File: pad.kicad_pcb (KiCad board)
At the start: 2 copper layers, 142.7 x 72.9 mm, 0 parts

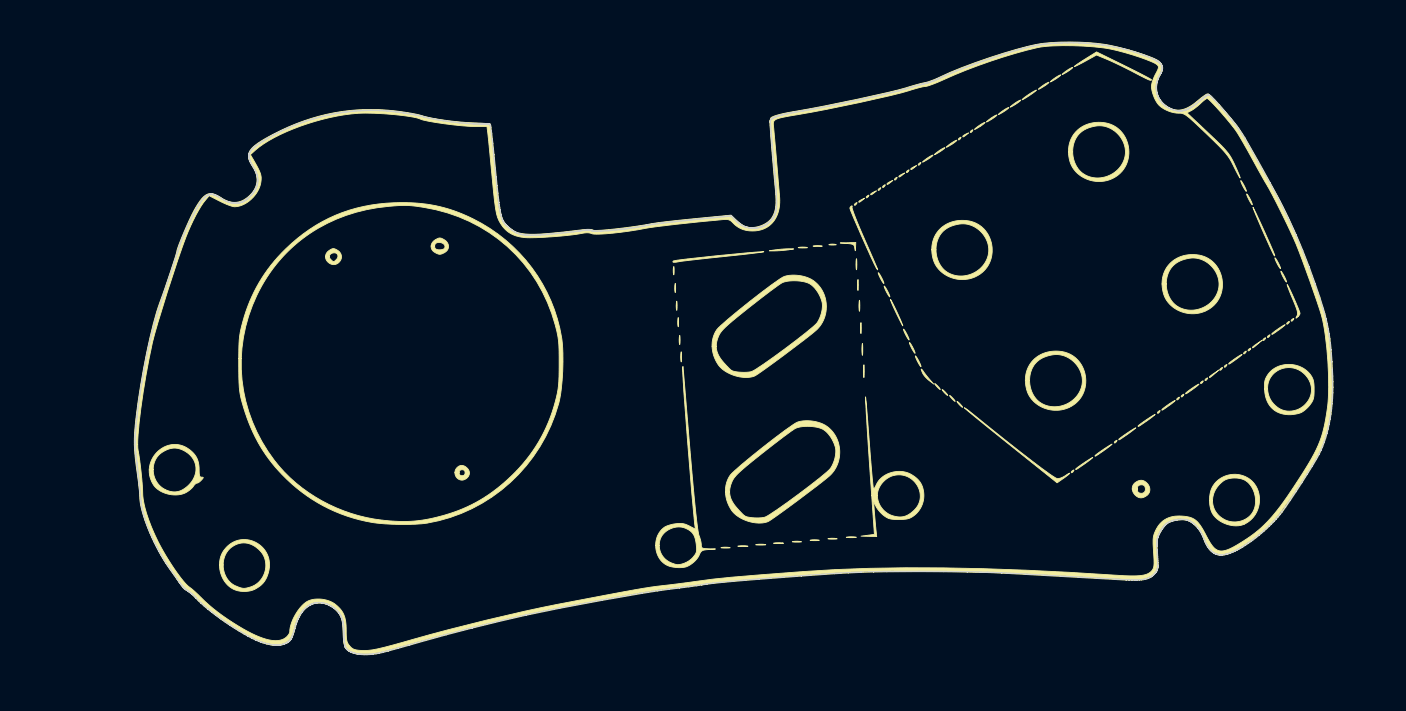
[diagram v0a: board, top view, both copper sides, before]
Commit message: Update schematic and board. All implemented, but not tested. Mechanical not tested yet
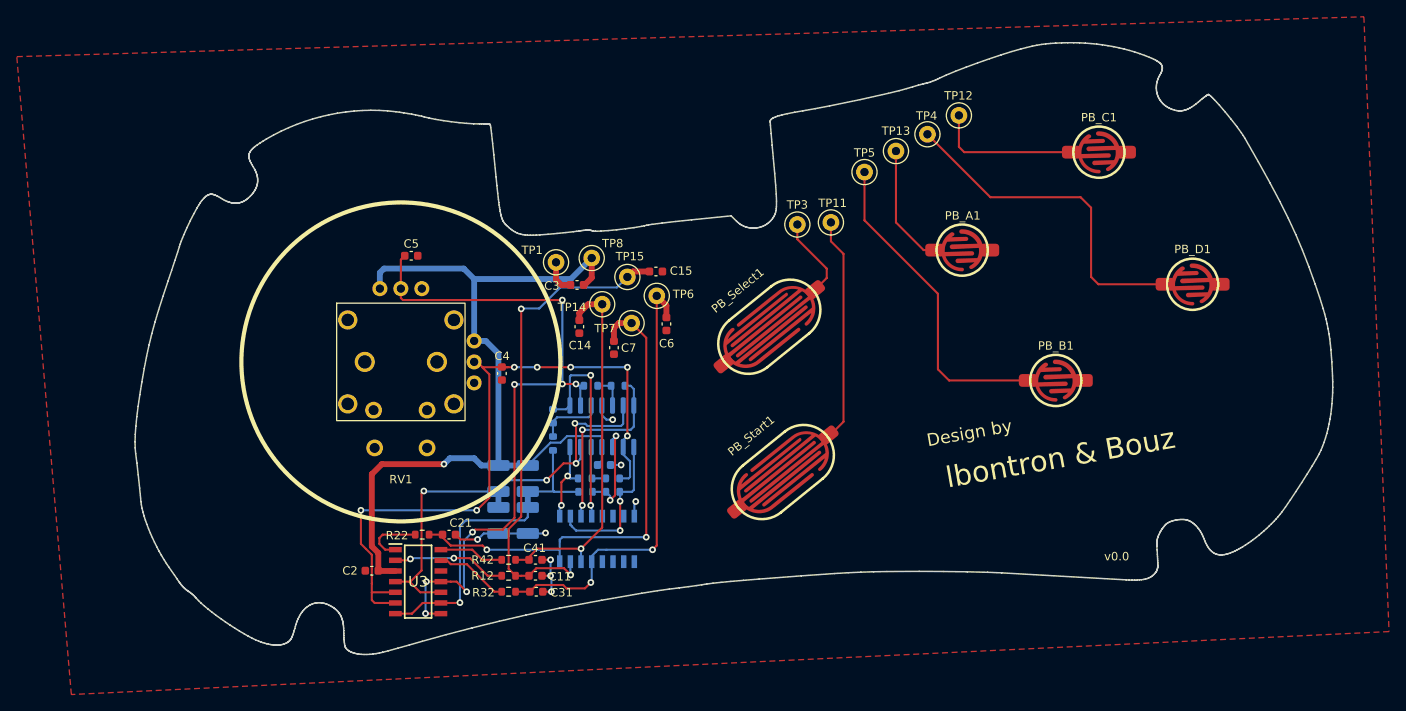
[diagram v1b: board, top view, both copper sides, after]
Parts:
- added C1: C, Capacitor_SMD:C_0603_1608Metric, B.Cu at (106.0, 100.4)
- added C11: C, Capacitor_SMD:C_0603_1608Metric, F.Cu at (97.8, 113.6)
- added C14: C, Capacitor_SMD:C_0603_1608Metric, F.Cu at (103.0, 83.9)
- added C15: C, Capacitor_SMD:C_0603_1608Metric, F.Cu at (112.2, 77.3)
- added C2: C, Capacitor_SMD:C_0603_1608Metric, F.Cu at (78.3, 113.0)
- added C21: C, Capacitor_SMD:C_0603_1608Metric, F.Cu at (87.5, 108.7)
- added C3: C, Capacitor_SMD:C_0603_1608Metric, F.Cu at (102.8, 79.0)
- added C31: C, Capacitor_SMD:C_0603_1608Metric, F.Cu at (97.9, 115.5)
- added C4: C, Capacitor_SMD:C_0603_1608Metric, F.Cu at (93.8, 89.5)
- added C41: C, Capacitor_SMD:C_0603_1608Metric, F.Cu at (97.8, 111.7)
- added C5: C, Capacitor_SMD:C_0603_1608Metric, F.Cu at (83.0, 75.5)
- added C6: C, Capacitor_SMD:C_0603_1608Metric, F.Cu at (113.4, 83.6)
- added C7: C, Capacitor_SMD:C_0603_1608Metric, F.Cu at (107.2, 86.4)
- added PB_A1: SW_Push, pad-button:button_A, F.Cu at (148.6, 74.8)
- added PB_B1: SW_Push, pad-button:button_A, F.Cu at (159.8, 90.3)
- added PB_C1: SW_Push, pad-button:button_A, F.Cu at (164.9, 63.1)
- added PB_D1: SW_Push, pad-button:button_A, F.Cu at (176.1, 78.9)
- added PB_Select1: SW_Push, pad-button:button_start, F.Cu at (125.7, 83.9)
- added PB_Start1: SW_Push, pad-button:button_start, F.Cu at (127.3, 101.2)
- added R1: R, Resistor_SMD:R_1210_3225Metric_Pad1.30x2.65mm_HandSolder, B.Cu at (93.4, 102.0)
- added R10: R, Resistor_SMD:R_0603_1608Metric, B.Cu at (103.8, 103.6)
- added R11: R, Resistor_SMD:R_0603_1608Metric, B.Cu at (107.0, 103.6)
- added R12: R, Resistor_SMD:R_0603_1608Metric, F.Cu at (94.6, 113.6)
- added R2: R, Resistor_SMD:R_1210_3225Metric_Pad1.30x2.65mm_HandSolder, B.Cu at (93.4, 107.0)
- added R20: R, Resistor_SMD:R_0603_1608Metric, B.Cu at (107.0, 102.0)
- added R21: R, Resistor_SMD:R_0603_1608Metric, B.Cu at (103.7, 102.0)
- added R22: R, Resistor_SMD:R_0603_1608Metric, F.Cu at (84.3, 108.7)
- added R3: R, Resistor_SMD:R_1210_3225Metric_Pad1.30x2.65mm_HandSolder, B.Cu at (96.9, 102.0)
- added R30: R, Resistor_SMD:R_0603_1608Metric, B.Cu at (99.9, 97.8)
- added R31: R, Resistor_SMD:R_0603_1608Metric, B.Cu at (99.9, 94.6)
- added R32: R, Resistor_SMD:R_0603_1608Metric, F.Cu at (94.6, 115.5)
- added R4: R, Resistor_SMD:R_1210_3225Metric_Pad1.30x2.65mm_HandSolder, B.Cu at (96.9, 107.0)
- added R40: R, Resistor_SMD:R_0603_1608Metric, B.Cu at (104.4, 91.0)
- added R41: R, Resistor_SMD:R_0603_1608Metric, B.Cu at (107.6, 91.0)
- added R42: R, Resistor_SMD:R_0603_1608Metric, F.Cu at (94.6, 111.7)
- added RV1: RKJXV122400R, pad-button:RKJXV122400R_joystick, F.Cu at (81.8, 88.1)
- added TP1: db15.1_GND, TestPoint:TestPoint_Loop_D1.80mm_Drill1.0mm_Beaded, F.Cu at (100.2, 76.2)
- added TP11: db15.11_Start, TestPoint:TestPoint_Loop_D1.80mm_Drill1.0mm_Beaded, F.Cu at (133.0, 71.5)
- added TP12: db15.12_ButtonC, TestPoint:TestPoint_Loop_D1.80mm_Drill1.0mm_Beaded, F.Cu at (148.2, 58.8)
- added TP13: db15.13_ButtonA, TestPoint:TestPoint_Loop_D1.80mm_Drill1.0mm_Beaded, F.Cu at (140.8, 63.0)
- added TP14: db15.14_Left, TestPoint:TestPoint_Loop_D1.80mm_Drill1.0mm_Beaded, F.Cu at (105.8, 81.2)
- added TP15: db15.15_Top, TestPoint:TestPoint_Loop_D1.80mm_Drill1.0mm_Beaded, F.Cu at (108.8, 78.0)
- added TP3: db15.3_Select, TestPoint:TestPoint_Loop_D1.80mm_Drill1.0mm_Beaded, F.Cu at (129.0, 71.8)
- added TP4: db15.4_ButtonD, TestPoint:TestPoint_Loop_D1.80mm_Drill1.0mm_Beaded, F.Cu at (144.5, 61.0)
- added TP5: db15.5_ButtonB, TestPoint:TestPoint_Loop_D1.80mm_Drill1.0mm_Beaded, F.Cu at (137.0, 65.5)
- added TP6: db15.6_Right, TestPoint:TestPoint_Loop_D1.80mm_Drill1.0mm_Beaded, F.Cu at (112.2, 80.2)
- added TP7: db15.7_Bottom, TestPoint:TestPoint_Loop_D1.80mm_Drill1.0mm_Beaded, F.Cu at (109.2, 83.5)
- added TP8: db15.8_5V, TestPoint:TestPoint_Loop_D1.80mm_Drill1.0mm_Beaded, F.Cu at (104.5, 75.8)
- added U1: LPV324MX, Package_SO:SOIC-14_3.9x8.7mm_P1.27mm, B.Cu at (105.7, 95.8)
- added U2: ULN2002, External:SOIC127P600X175-16N, B.Cu at (105.1, 109.2)
- added U3: LM339, External:SOIC127P600X175-14N, F.Cu at (83.8, 114.3)
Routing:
- net +5V: track 0.00 -> 104.3 mm, vias 0 -> 1
- net yAxis: track 0.00 -> 85.8 mm, vias 0 -> 8
- net xAxis: track 0.00 -> 83.0 mm, vias 0 -> 7
- net TP7_BOT: track 0.00 -> 59.7 mm, vias 0 -> 2
- net TP15_TOP: track 0.00 -> 58.8 mm, vias 0 -> 2
- net VRef_p: track 0.00 -> 54.1 mm, vias 0 -> 4
- net TP6_RIG: track 0.00 -> 54.0 mm, vias 0 -> 2
- net TP14_LEF: track 0.00 -> 44.3 mm, vias 0 -> 1
- net Net-(PB_D1-Pad2): track 0.00 -> 40.6 mm
- net VRef_n: track 0.00 -> 40.0 mm, vias 0 -> 1
- net Net-(PB_B1-Pad2): track 0.00 -> 38.5 mm
- net GND: track 0.00 -> 27.9 mm, vias 0 -> 8
- net Net-(PB_Start1-Pad2): track 0.00 -> 26.8 mm
- net RigButton: track 0.00 -> 25.0 mm, vias 0 -> 2
- net LefButton: track 0.00 -> 22.3 mm, vias 0 -> 2
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- added copper zone on F.Cu, net GND
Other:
- board text added: "Design by"
- board text added: "lbontron & Bouz"
- board text added: "v0.0"
